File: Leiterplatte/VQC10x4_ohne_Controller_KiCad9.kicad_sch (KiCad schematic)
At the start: 34 parts, among them J2 Conn_02x10_Odd_Even, J3 Conn_02x10_Odd_Even, Q1 BD140, Q2 BD140, Q3 BD140, Q4 BD140, Q5 BD140, Q6 BD140, Q7 BD140, U1 74HCT138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

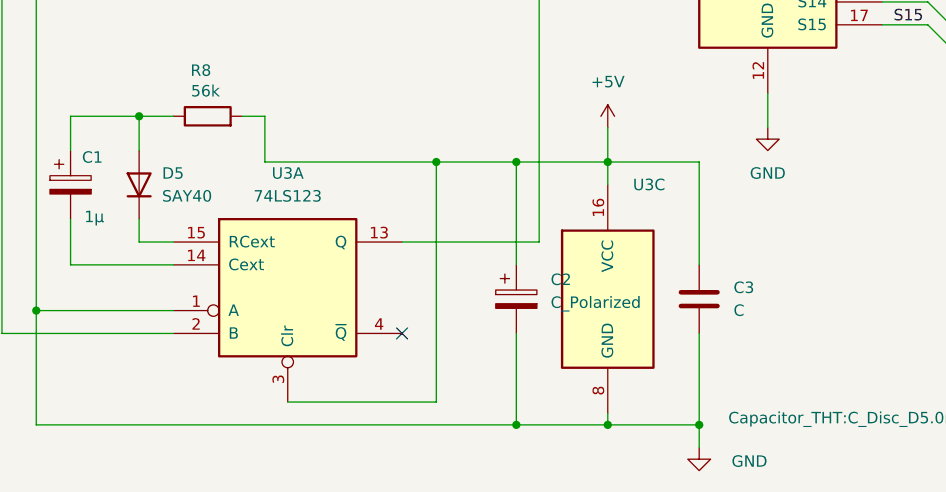
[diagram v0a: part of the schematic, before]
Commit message: Update Schaltplan + PDF
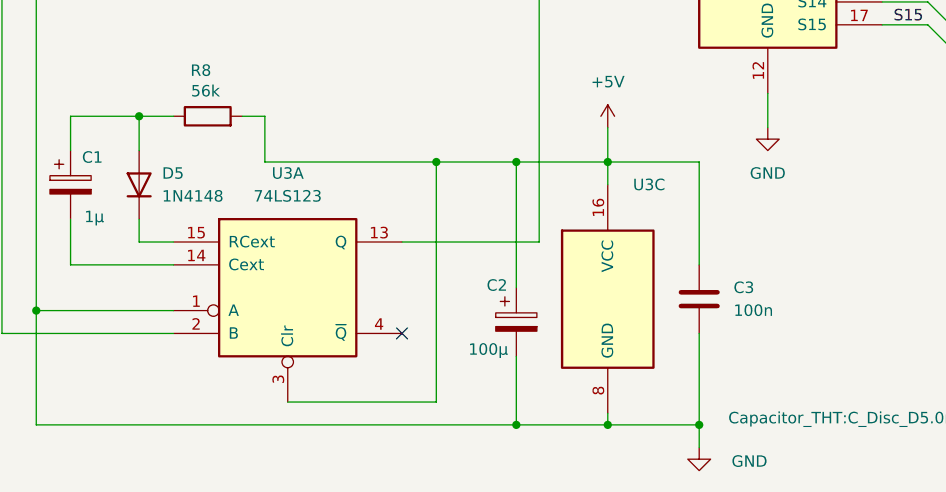
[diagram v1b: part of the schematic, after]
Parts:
- C2: value C_Polarized -> 100µ
- C3: value C -> 100n
- D5: value SAY40 -> 1N4148
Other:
- moved on the sheet: C2
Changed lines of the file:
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@@
 	(wire
 		(pts
-			(xy 72.39 180.34) (xy 72.39 190.5)
+			(xy 72.39 182.88) (xy 72.39 190.5)
 		)
 		(stroke
@@
 	(wire
 		(pts
-			(xy 72.39 172.72) (xy 72.39 161.29)
+			(xy 72.39 175.26) (xy 72.39 161.29)
 		)
 		(stroke
@@
 	(symbol
 		(lib_id "Device:C_Polarized")
-		(at 72.39 176.53 0)
+		(at 72.39 179.07 0)
 		(unit 1)
 		(exclude_from_sim no)
@@
 		(on_board yes)
 		(dnp no)
-		(fields_autoplaced yes)
 		(property "Reference" "C2"
-			(at 76.2 174.3709 0)
+			(at 69.088 175.006 0)
 			(effects
 				(font
@@
 			)
 		)
-		(property "Value" "C_Polarized"
-			(at 76.2 176.9109 0)
+		(property "Value" "100µ"
+			(at 67.056 182.118 0)
 			(effects
 				(font
@@
 		)
 		(property "Footprint" "Capacitor_THT:CP_Radial_D6.3mm_P2.50mm"
-			(at 73.3552 180.34 0)
+			(at 73.3552 182.88 0)
 			(effects
 				(font
@@
 		)
 		(property "Datasheet" "~"
-			(at 72.39 176.53 0)
+			(at 72.39 179.07 0)
 			(effects
 				(font
@@
 		)
 		(property "Description" "Polarized capacitor"
-			(at 72.39 176.53 0)
+			(at 72.39 179.07 0)
 			(effects
 				(font
@@
 			)
 		)
-		(property "Value" "SAY40"
+		(property "Value" "1N4148"
 			(at 33.02 165.0999 90)
 			(effects
@@
 			)
 		)
-		(property "Value" "C"
+		(property "Value" "100n"
 			(at 96.52 177.7999 0)
 			(effects
